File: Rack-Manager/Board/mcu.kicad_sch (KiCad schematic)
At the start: 1 part, among them U6 STM32G0B1KCUx

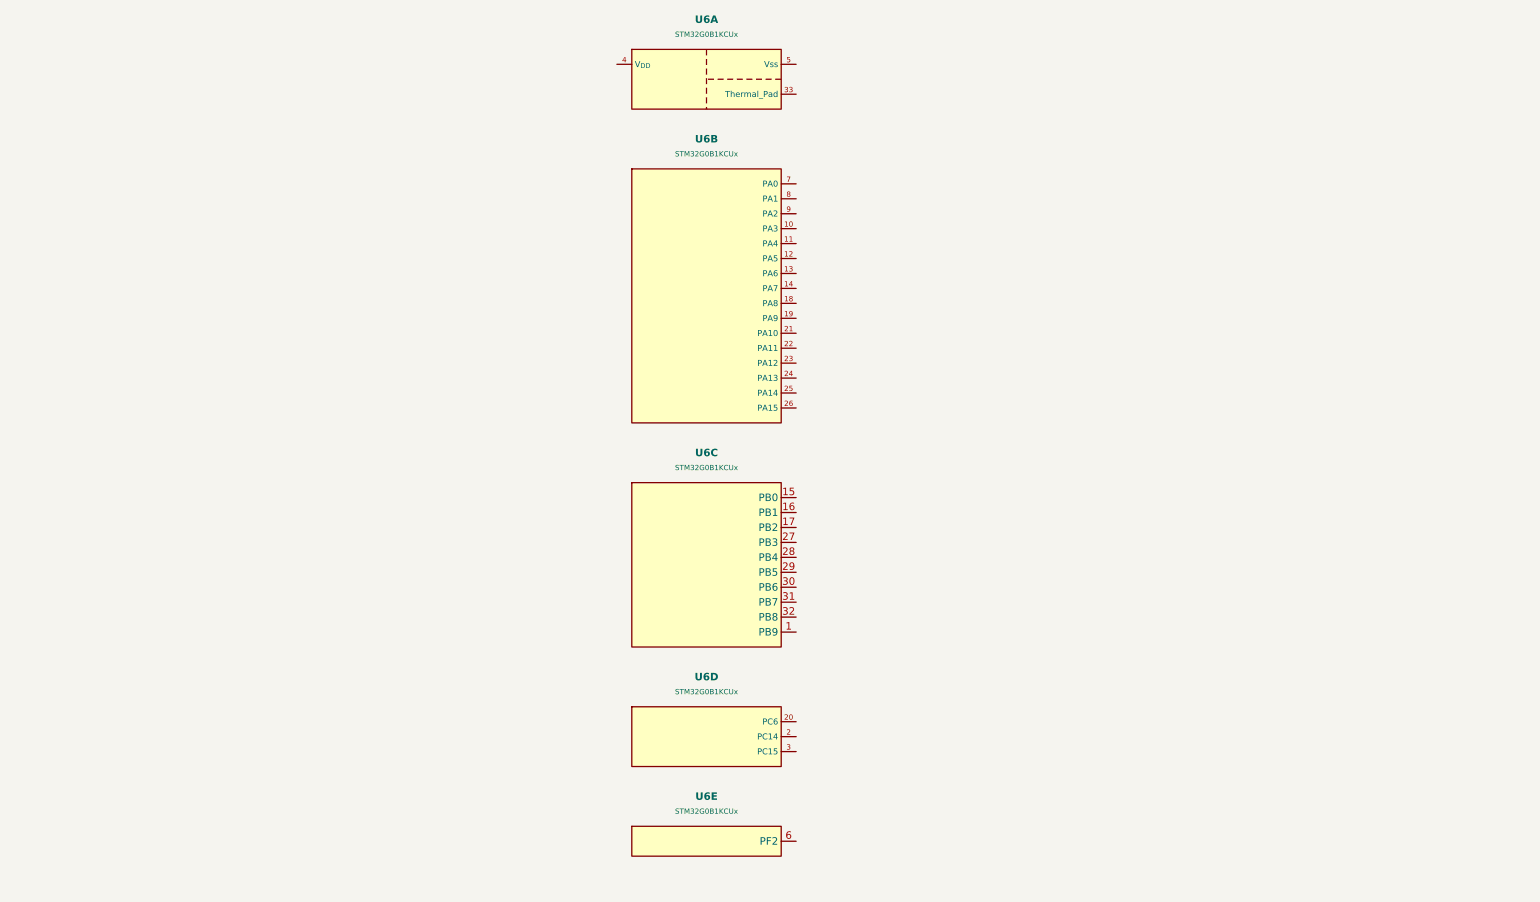
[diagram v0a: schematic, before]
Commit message: Updated Texas Instruments and WIZnet KiCAD libraries. Continued with the schematics design.
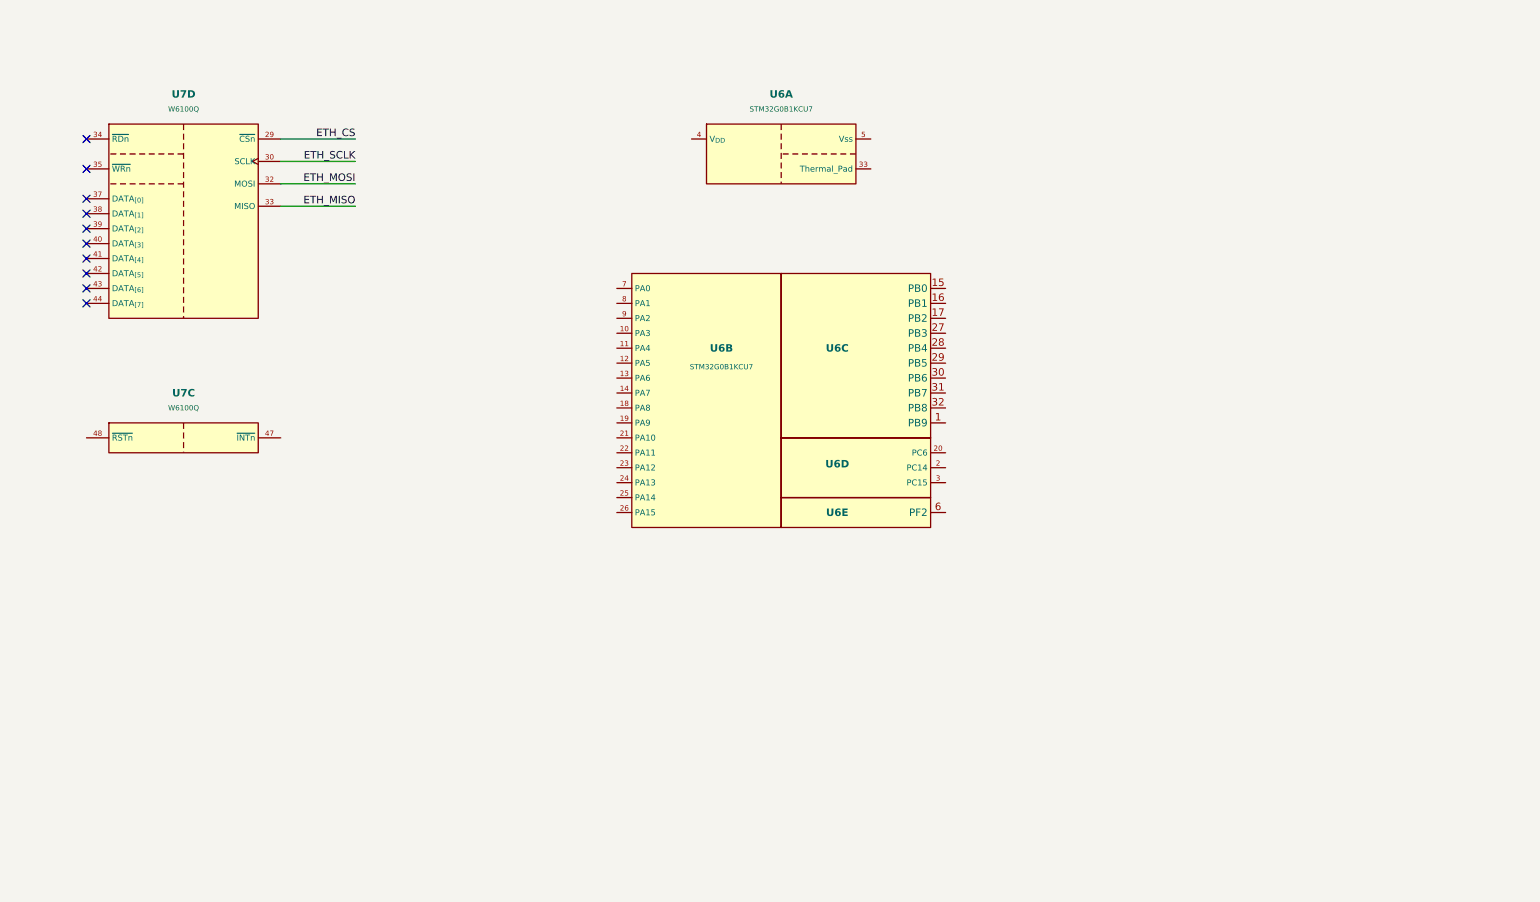
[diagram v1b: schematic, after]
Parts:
- added U7: W6100Q, WIZnet:QFN-48 (Thermal Pad), symbol WIZnet:W6100Q
- U6: value STM32G0B1KCUx -> STM32G0B1KCU7; JLCPCB # (none) -> C5270235; Mouser Link (none) -> https://www.mouser.it/ProductDetail/511-STM32G0B1KCU7
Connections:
- new net ETH_CS: U7.29 (~{CSn})
- new net ETH_MISO: U7.33 (MISO)
- new net ETH_MOSI: U7.32 (MOSI)
- new net ETH_SCLK: U7.30 (SCLK)
- no-connect marks 0 -> 10
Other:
- moved on the sheet: U6A, U6B, U6C, U6D, U6E

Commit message: Updated Texas Instruments KiCAD library. Continued with the schematics design.
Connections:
- net ~{ETH_INT}: now reaches U7.47 (~{INTn})
- net ~{ETH_RST}: now reaches U7.48 (~{RSTn})
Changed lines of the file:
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@@
+	(wire
+		(pts
+			(xy 114.3 78.74) (xy 101.6 78.74)
+		)
+		(stroke
+			(width 0)
+			(type default)
+		)
+	)
 	(wire
 		(pts
 			(xy 67.31 57.15) (xy 80.01 57.15)
+		)
+		(stroke
+			(width 0)
+			(type default)
+		)
+	)
+	(wire
+		(pts
+			(xy 114.3 86.36) (xy 101.6 86.36)
+		)
+		(stroke
+			(width 0)
+			(type default)
+		)
+	)
+	(wire
+		(pts
+			(xy 114.3 82.55) (xy 101.6 82.55)
+		)
+		(stroke
+			(width 0)
+			(type default)
+		)
+	)
+	(wire
+		(pts
+			(xy 34.29 104.14) (xy 21.59 104.14)
+		)
+		(stroke
+			(width 0)
+			(type default)
+		)
+	)
+	(wire
+		(pts
+			(xy 67.31 104.14) (xy 80.01 104.14)
 		)
 		(stroke
@@
 		)
 	)
+	(wire
+		(pts
+			(xy 114.3 90.17) (xy 101.6 90.17)
+		)
+		(stroke
+			(width 0)
+			(type default)
+		)
+	)
+	(label "~{ETH_INT}"
+		(at 80.01 104.14 180)
+		(effects
+			(font
+				(size 1.016 1.016)
+			)
+			(justify right bottom)
+		)
+	)
+	(label "~{ETH_RST}"
+		(at 21.59 104.14 0)
+		(effects
+			(font
+				(size 1.016 1.016)
+			)
+			(justify left bottom)
+		)
+	)
+	(label "ETH_SCLK"
+		(at 101.6 82.55 0)
+		(effects
+			(font
+				(size 1.016 1.016)
+			)
+			(justify left bottom)
+		)
+	)
 	(label "ETH_MOSI"
 		(at 80.01 60.96 180)
 		(effects
 			(font
-				(size 1.27 1.27)
+				(size 1.016 1.016)
 			)
 			(justify right bottom)
+		)
+	)
+	(label "ETH_MOSI"
+		(at 101.6 86.36 0)
+		(effects
+			(font
+				(size 1.016 1.016)
+			)
+			(justify left bottom)
+		)
+	)
+	(label "ETH_CS"
+		(at 101.6 78.74 0)
+		(effects
+			(font
+				(size 1.016 1.016)
+			)
+			(justify left bottom)
 		)
 	)
@@
 		(effects
 			(font
-				(size 1.27 1.27)
+				(size 1.016 1.016)
 			)
 			(justify right bottom)
@@
 		(effects
 			(font
-				(size 1.27 1.27)
+				(size 1.016 1.016)
 			)
 			(justify right bottom)
@@
 		(effects
 			(font
-				(size 1.27 1.27)
+				(size 1.016 1.016)
 			)
 			(justify right bottom)
 		)
 	)
+	(label "ETH_MISO"
+		(at 101.6 90.17 0)
+		(effects
+			(font
+				(size 1.016 1.016)
+			)
+			(justify left bottom)
+		)
+	)

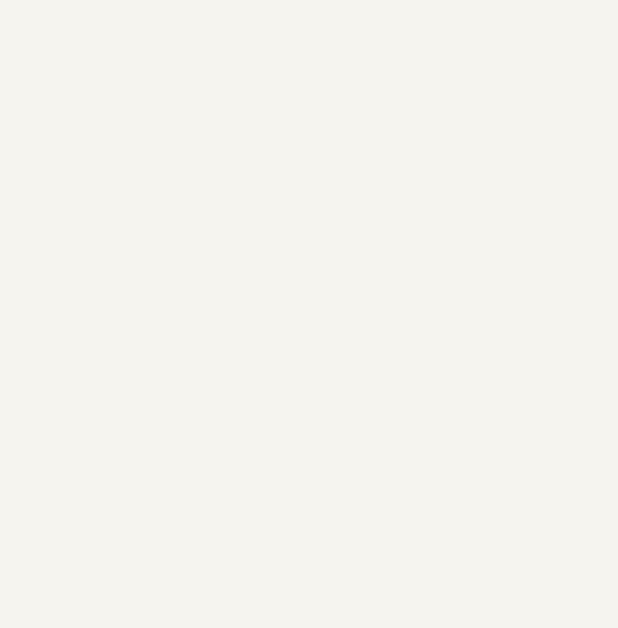
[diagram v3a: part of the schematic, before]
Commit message: Fixed volteage divider for fan tachometer and fixed other pull-x and divider for the microcontroller
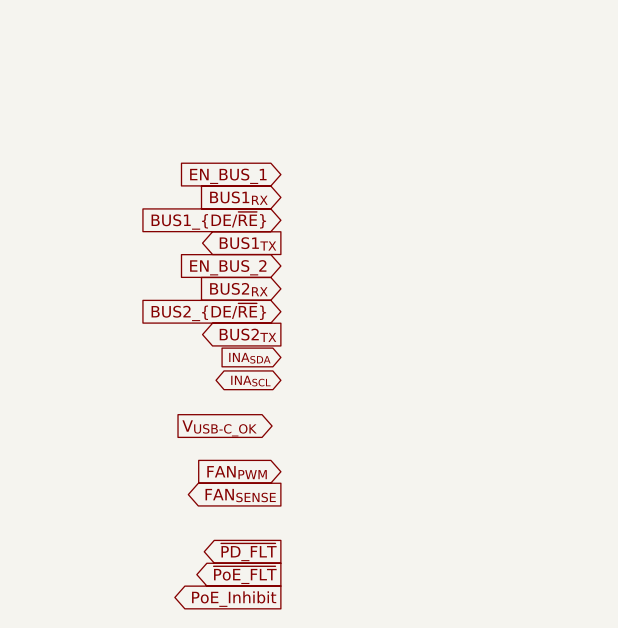
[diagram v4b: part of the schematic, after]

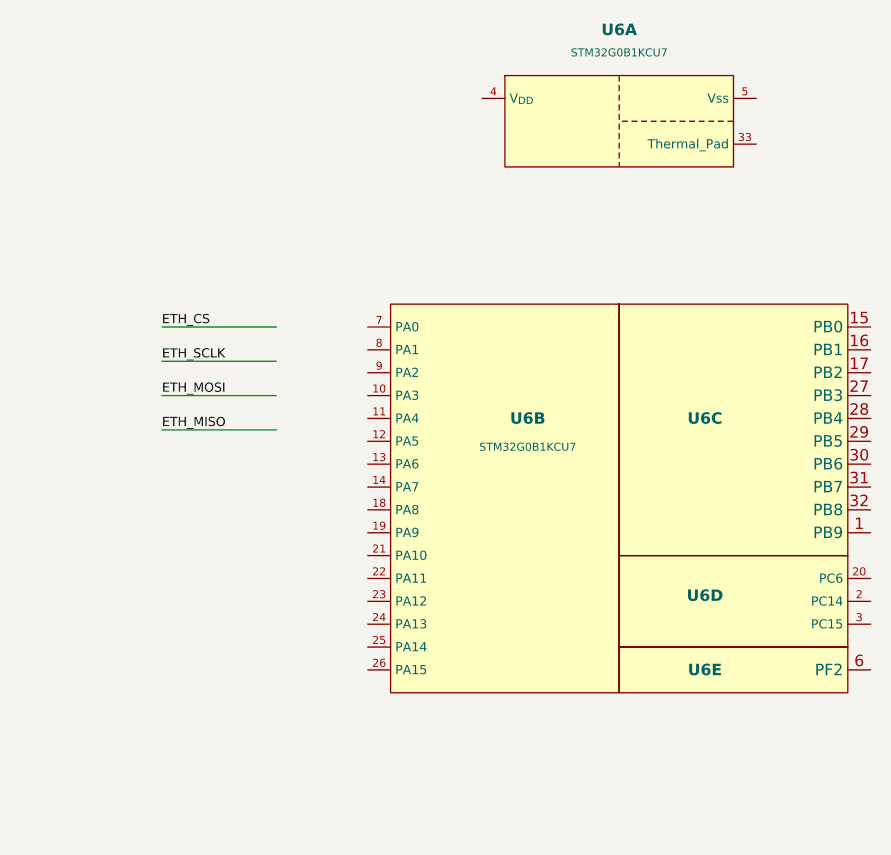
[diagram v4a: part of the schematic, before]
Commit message: Found some error or missing stuff and noted on the main sheet
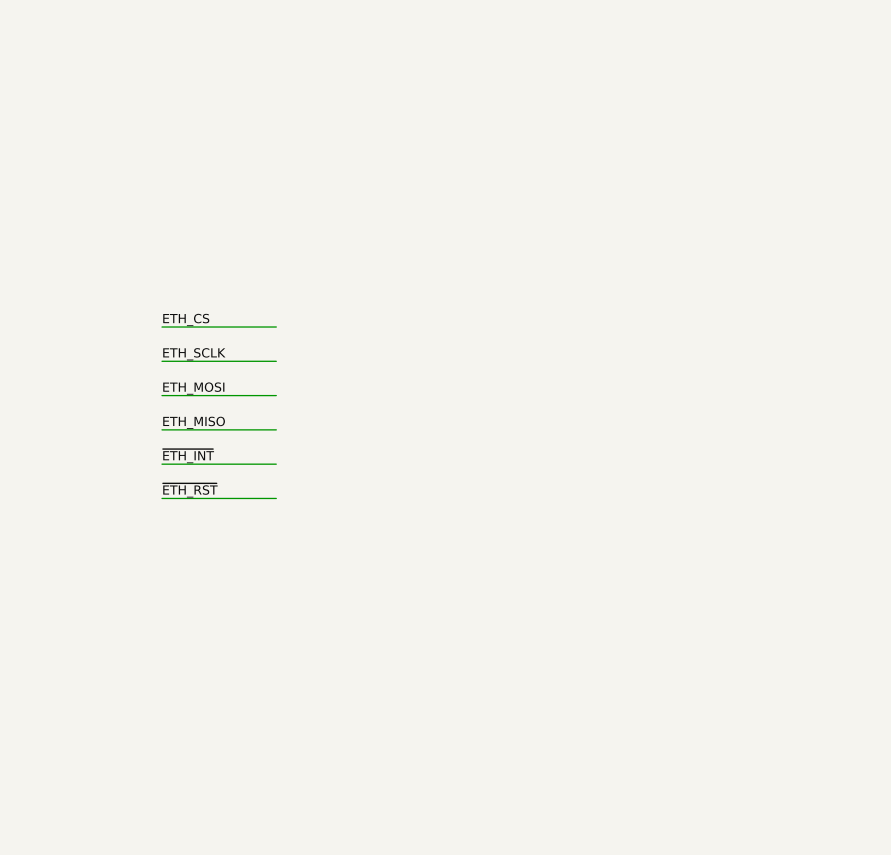
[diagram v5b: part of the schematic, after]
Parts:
- removed U6: STM32G0B1KCU7, Package_DFN_QFN:QFN-32-1EP_5x5mm_P0.5mm_EP3.45x3.45mm, symbol STMicroelectronics:STM32G0B1KCUx

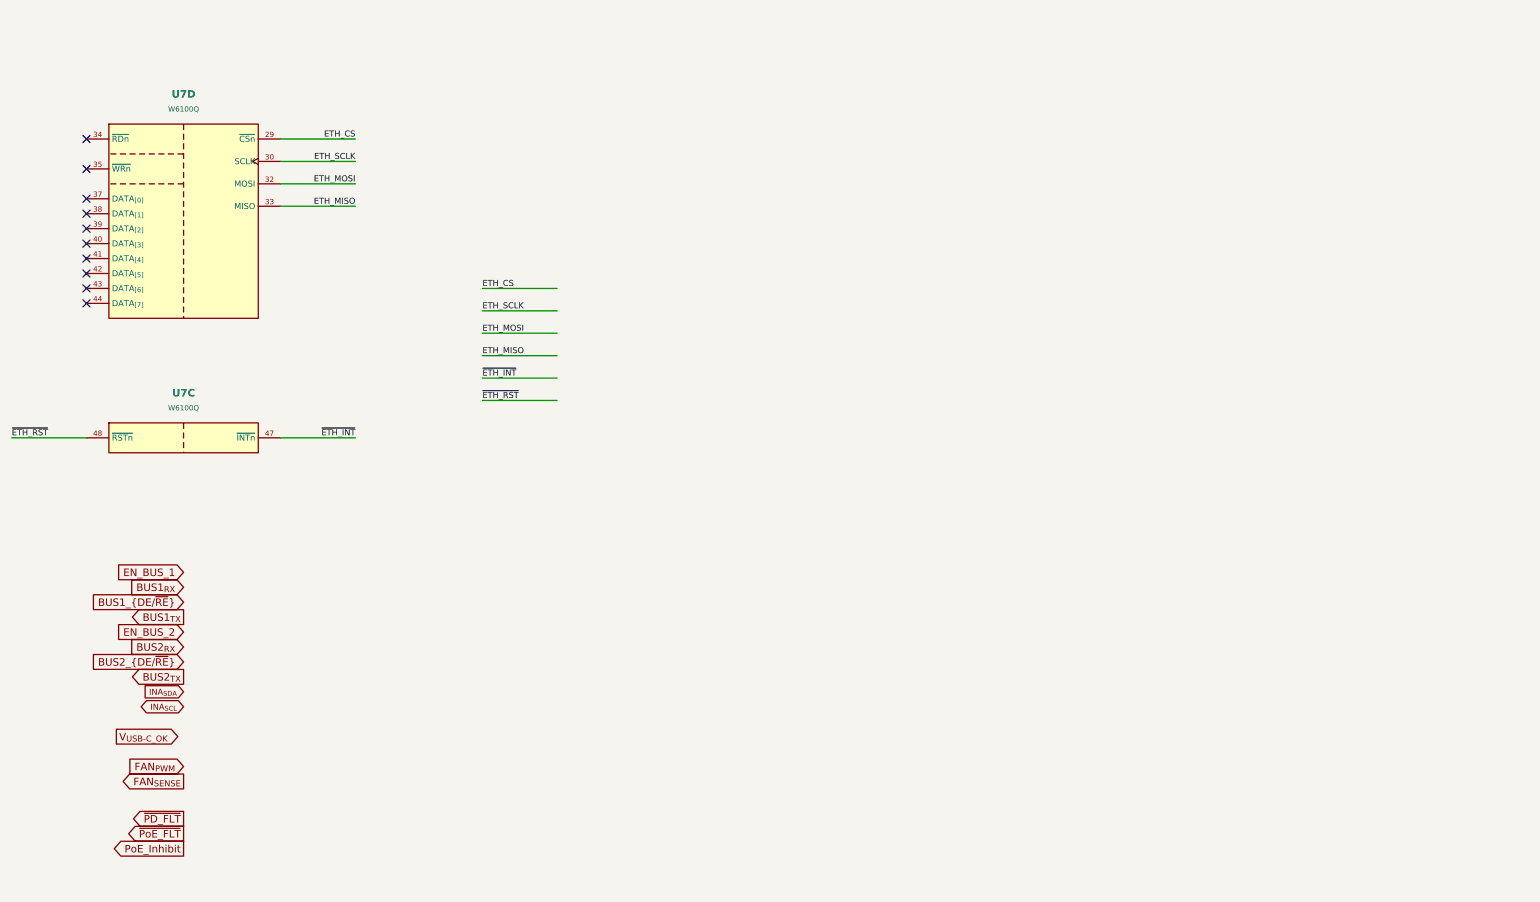
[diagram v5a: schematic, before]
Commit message: Added MCU, Fixed USB-C PD Ideal Diode bug and updated the todo notes
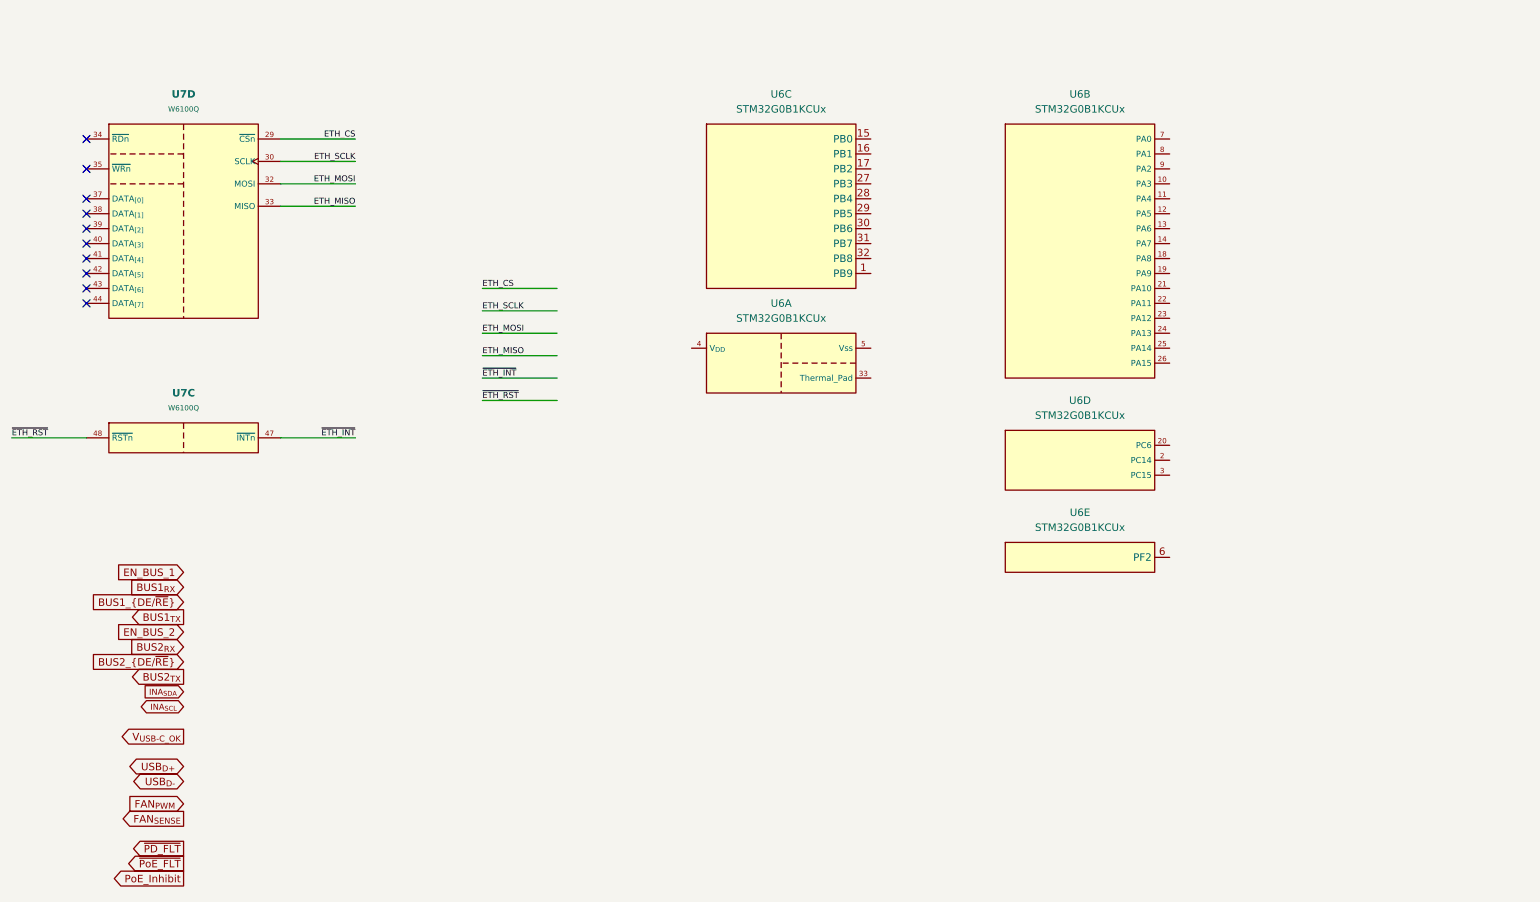
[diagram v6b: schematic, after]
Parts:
- added U6: STM32G0B1KCUx, Package_DFN_QFN:QFN-32-1EP_5x5mm_P0.5mm_EP3.45x3.45mm, symbol STMicroelectronics:STM32G0B1KCUx

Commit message: Some fix and kicad update
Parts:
- added C38, C39: 12.5pF, symbol Device:C_Small
- added JP2: ~, TestPoint:TestPoint_2Pads_Pitch2.54mm_Drill0.8mm, symbol Jumper:Jumper_2_Open
- added R74: 10k, Resistor_SMD:R_0201_0603Metric, symbol Device:R_Small_US
- added Y3: 32.768kHz, Crystal:Crystal_SMD_Abracon_ABS25-4Pin_8.0x3.8mm, symbol Device:Crystal_GND23
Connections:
- net OSC_IN: now reaches U6.2 (PC14)
- net OSC_IN: now also C38.1, Y3.1
- net OSC_OUT: now reaches U6.3 (PC15)
- net OSC_OUT: now also C39.1, Y3.4
- net BOOT: now reaches U6.25 (PA14)
- net BOOT: now also JP2.1 (A), R74.2
- net GND: now reaches U6.33 (Thermal_Pad)
- net GND: now also U6.5 (Vss), C38.2, C39.2, R74.1, Y3.2 (G), Y3.3 (G)
- net 3V3: now reaches U6.4 (V_{DD})
- net 3V3: now also JP2.2 (B)
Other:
- moved on the sheet: U6A, U6D
